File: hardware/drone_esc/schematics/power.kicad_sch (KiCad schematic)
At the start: 0 parts

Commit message: created power schematics, assigned footprints and parts
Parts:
- added C1, C2: 22uF 25V X7R MLCC, Capacitor_SMD:C_1210_3225Metric, symbol Device:C
- added C3: 100nF 10V X7R MLCC, Capacitor_SMD:C_0402_1005Metric, symbol Device:C
- added C4: 1nF 10V X7R MLCC, Capacitor_SMD:C_0402_1005Metric, symbol Device:C
- added R1: 1k, Resistor_SMD:R_0402_1005Metric, symbol Device:R
- added U1: AMS1117-3.3, Package_TO_SOT_SMD:SOT-223-3_TabPin2, symbol Regulator_Linear:AMS1117-3.3
- added U2: INA180A3, Package_TO_SOT_SMD:SOT-23-5, symbol Amplifier_Current:INA180A3
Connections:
- new net: C4.1, R1.2
- new net: R1.1, U2.1
- new net +3.3V: C2.1, C3.1, U1.2 (VO), U2.5 (V+)
- new net GND: C1.2, C2.2, C3.2, C4.2, U1.1 (GND), U2.2 (GND), U2.4 (-)
- new net VCC: C1.1, U1.3 (VI), U2.3 (+)
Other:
- note added: "100A: P = I^{2}R = 100A^{2} 0.00025 = 100A: 0.00025 100 ="
- note added: "Current Sense"
- note added: "Linear regulator (VCC to 3.3v)"
- note added: "Power"
- note added: "VCC = 4S"

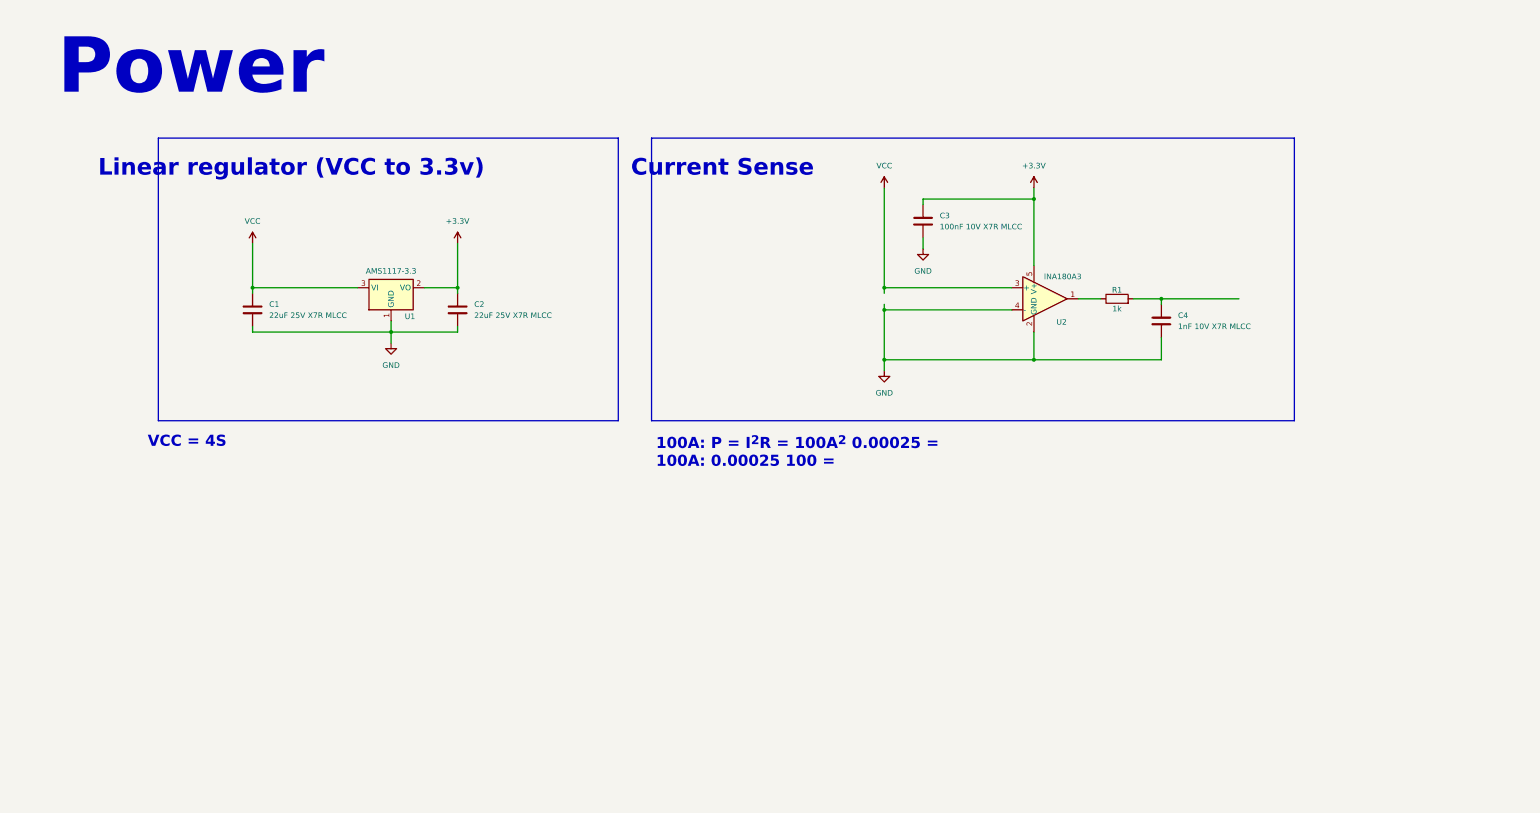
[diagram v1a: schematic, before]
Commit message: finished power section and one esc. need to finish the component assinment for jlcpcb and the rest of the esc
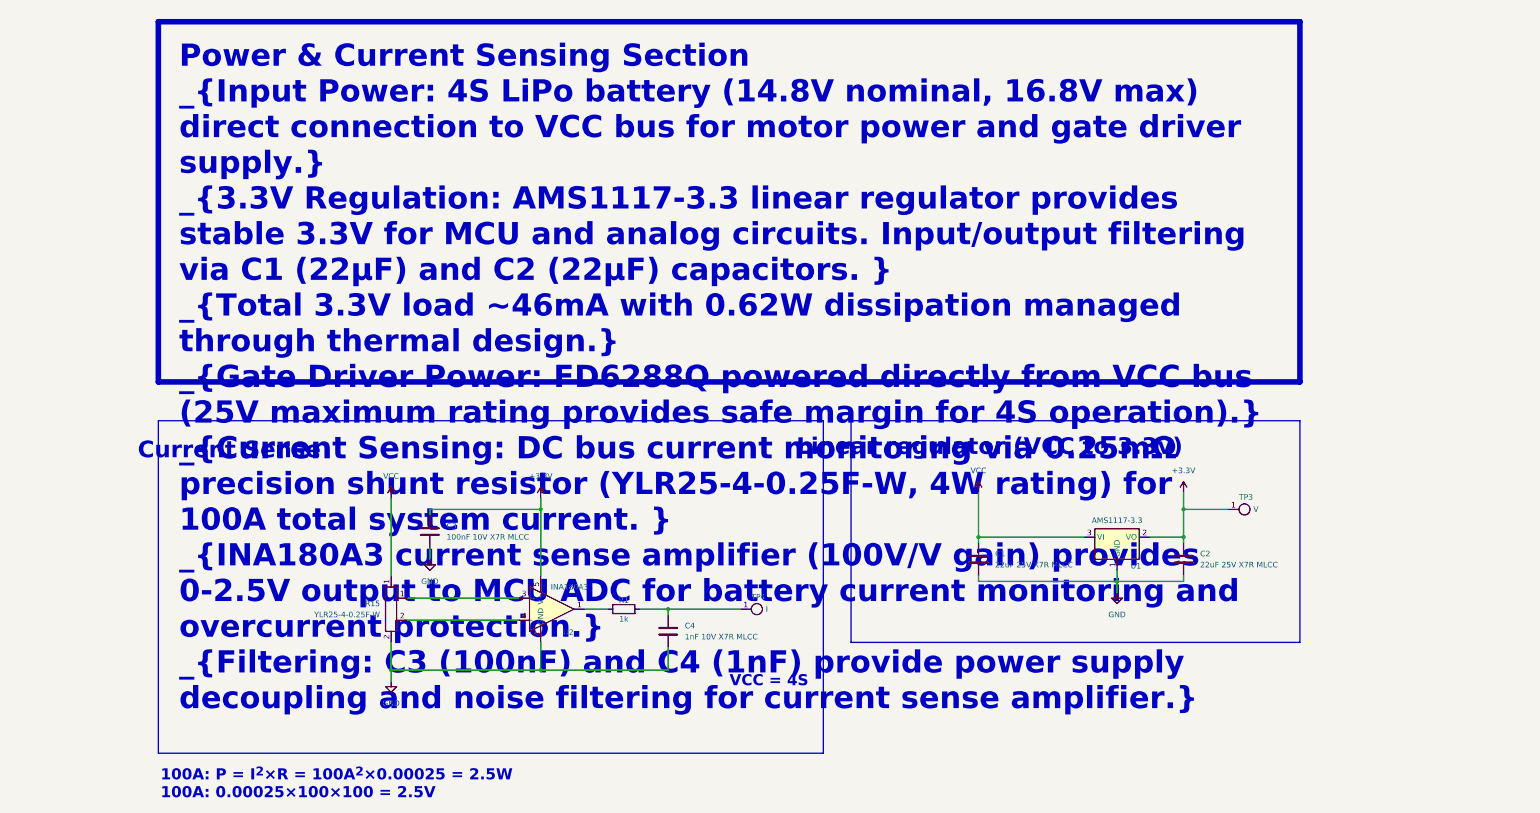
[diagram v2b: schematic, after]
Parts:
- added R15: YLR25-4-0.25F-W, Drone_components:YLR25-4-0.25F-W, symbol Drone_components:YLR25-4-0.25F-W
- added TP3: V, Drone_components:Rectangle test point, symbol Drone_components:Rectangle_test_point
- added TP4: I, Drone_components:Rectangle test point, symbol Drone_components:Rectangle_test_point
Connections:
- net +3.3V: now also TP3.1
- net GND: now also R15.2; no longer U2.4 (-)
- net VCC: now also R15.1; no longer U2.3 (+)
- net at C4.1, R1.2: now also TP4.1
- new net: R15.1, U2.3 (+)
- new net: R15.2, U2.4 (-)
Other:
- note added: "100A: P = I^{2}×R = 100A^{2}×0.00025 = 2.5W 100A: 0.00025×100×100 = 2.5V"
- note removed: "100A: P = I^{2}R = 100A^{2} 0.00025 = 100A: 0.00025 100 ="
- note removed: "Power"
- moved on the sheet: C1, C2, C3, C4, R1, U1, U2

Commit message: continued developing the pcb board
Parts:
- C1, C2: value 22uF 25V X7R MLCC -> 22uF 25V X5R MLCC; JLCPCB part C309062 -> C12891
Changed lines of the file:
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@@
+	)
+	(symbol
+		(lib_id "Device:C")
+		(at 252.73 140.97 0)
+		(unit 1)
+		(exclude_from_sim no)
+		(in_bom yes)
+		(on_board yes)
+		(dnp no)
+		(fields_autoplaced yes)
+		(property "Reference" "C2"
+			(at 256.54 139.6999 0)
+			(effects
+				(font
+					(size 1.27 1.27)
+				)
+				(justify left)
+			)
+		)
+		(property "Value" "22uF 25V X5R MLCC"
+			(at 256.54 142.2399 0)
+			(effects
+				(font
+					(size 1.27 1.27)
+				)
+				(justify left)
+			)
+		)
+		(property "Footprint" "Capacitor_SMD:C_1210_3225Metric"
+			(at 253.6952 144.78 0)
+			(effects
+				(font
+					(size 1.27 1.27)
+				)
+				(hide yes)
+			)
+		)
+		(property "Datasheet" "~"
+			(at 252.73 140.97 0)
+			(effects
+				(font
+					(size 1.27 1.27)
+				)
+				(hide yes)
+			)
+		)
+		(property "Description" "Unpolarized capacitor"
+			(at 252.73 140.97 0)
+			(effects
+				(font
+					(size 1.27 1.27)
+				)
+				(hide yes)
+			)
+		)
+		(property "JLCPCB part" "C12891"
+			(at 252.73 140.97 0)
+			(effects
+				(font
+					(size 1.27 1.27)
+				)
+				(hide yes)
+			)
+		)
+		(pin "2"
+		)
+		(pin "1"
+		)
+		(instances
+			(project "drone_esc"
+				(path "/b5a13fd4-6868-4fff-a56c-eae40f1d53c7/2b3d35f8-ad3a-479e-afa3-88f04276a871"
+					(reference "C2")
+					(unit 1)
+				)
+			)
+		)
 	)
 	(symbol
@@
 	(symbol
 		(lib_id "Device:C")
+		(at 205.74 140.97 0)
+		(unit 1)
+		(exclude_from_sim no)
+		(in_bom yes)
+		(on_board yes)
+		(dnp no)
+		(fields_autoplaced yes)
+		(property "Reference" "C1"
+			(at 209.55 139.6999 0)
+			(effects
+				(font
+					(size 1.27 1.27)
+				)
+				(justify left)
+			)
+		)
+		(property "Value" "22uF 25V X5R MLCC"
+			(at 209.55 142.2399 0)
+			(effects
+				(font
+					(size 1.27 1.27)
+				)
+				(justify left)
+			)
+		)
+		(property "Footprint" "Capacitor_SMD:C_1210_3225Metric"
+			(at 206.7052 144.78 0)
+			(effects
+				(font
+					(size 1.27 1.27)
+				)
+				(hide yes)
+			)
+		)
+		(property "Datasheet" "~"
+			(at 205.74 140.97 0)
+			(effects
+				(font
+					(size 1.27 1.27)
+				)
+				(hide yes)
+			)
+		)
+		(property "Description" "Unpolarized capacitor"
+			(at 205.74 140.97 0)
+			(effects
+				(font
+					(size 1.27 1.27)
+				)
+				(hide yes)
+			)
+		)
+		(property "JLCPCB part" "C12891"
+			(at 205.74 140.97 0)
+			(effects
+				(font
+					(size 1.27 1.27)
+				)
+				(hide yes)
+			)
+		)
+		(pin "2"
+		)
+		(pin "1"
+		)
+		(instances
+			(project "drone_esc"
+				(path "/b5a13fd4-6868-4fff-a56c-eae40f1d53c7/2b3d35f8-ad3a-479e-afa3-88f04276a871"
+					(reference "C1")
+					(unit 1)
+				)
+			)
+		)
+	)
+	(symbol
+		(lib_id "Device:C")
 		(at 134.62 157.48 0)
 		(unit 1)
@@
 	)
 	(symbol
-		(lib_id "Device:C")
-		(at 205.74 140.97 0)
-		(unit 1)
-		(exclude_from_sim no)
-		(in_bom yes)
-		(on_board yes)
-		(dnp no)
-		(fields_autoplaced yes)
-		(property "Reference" "C1"
-			(at 209.55 139.6999 0)
-			(effects
-				(font
-					(size 1.27 1.27)
-				)
-				(justify left)
-			)
-		)
-		(property "Value" "22uF 25V X7R MLCC"
-			(at 209.55 142.2399 0)
-			(effects
-				(font
-					(size 1.27 1.27)
-				)
-				(justify left)
-			)
-		)
-		(property "Footprint" "Capacitor_SMD:C_1210_3225Metric"
-			(at 206.7052 144.78 0)
-			(effects
-				(font
-					(size 1.27 1.27)
-				)
-				(hide yes)
-			)
-		)
-		(property "Datasheet" "https://lcsc.com/datasheet/lcsc_datasheet_2304140030_Samsung-Electro-Mechanics-CL32B226KAJNNNE_C309062.pdf"
-			(at 205.74 140.97 0)
-			(effects
-				(font
-					(size 1.27 1.27)
-				)
-				(hide yes)
-			)
-		)
-		(property "Description" "Unpolarized capacitor"
-			(at 205.74 140.97 0)
-			(effects
-				(font
-					(size 1.27 1.27)
-				)
-				(hide yes)
-			)
-		)
-		(property "JLCPCB part" "C309062"
-			(at 205.74 140.97 0)
-			(effects
-				(font
-					(size 1.27 1.27)
-				)
-				(hide yes)
-			)
-		)
-		(pin "1"
-		)
-		(pin "2"
-		)
-		(instances
-			(project ""
-				(path "/b5a13fd4-6868-4fff-a56c-eae40f1d53c7/2b3d35f8-ad3a-479e-afa3-88f04276a871"
-					(reference "C1")
-					(unit 1)
-				)
-			)
-		)
-	)
-	(symbol
 		(lib_id "Regulator_Linear:AMS1117-3.3")
 		(at 237.49 135.89 0)
@@
 					(unit 1)
 				)
-			)
-		)
-	)
-	(symbol
-		(lib_id "Device:C")
-		(at 252.73 140.97 0)
-		(unit 1)
-		(exclude_from_sim no)
-		(in_bom yes)
-		(on_board yes)
-		(dnp no)
-		(fields_autoplaced yes)
-		(property "Reference" "C2"
-			(at 256.54 139.6999 0)
-			(effects
-				(font
-					(size 1.27 1.27)
-				)
-				(justify left)
-			)
-		)
-		(property "Value" "22uF 25V X7R MLCC"
-			(at 256.54 142.2399 0)
-			(effects
-				(font
-					(size 1.27 1.27)
-				)
-				(justify left)
-			)
-		)
-		(property "Footprint" "Capacitor_SMD:C_1210_3225Metric"
-			(at 253.6952 144.78 0)
-			(effects
-				(font
-					(size 1.27 1.27)
-				)
-				(hide yes)
-			)
-		)
-		(property "Datasheet" "~"
-			(at 252.73 140.97 0)
-			(effects
-				(font
-					(size 1.27 1.27)
-				)
-				(hide yes)
-			)
-		)
-		(property "Description" "Unpolarized capacitor"
-			(at 252.73 140.97 0)
-			(effects
-				(font
-					(size 1.27 1.27)
-				)
-				(hide yes)
-			)
-		)
-		(property "JLCPCB part" "C309062"
-			(at 252.73 140.97 0)
-			(effects
-				(font
-					(size 1.27 1.27)
-				)
-				(hide yes)
-			)
-		)
-		(pin "1"
-		)
-		(pin "2"
-		)
-		(instances
-			(project "drone_esc"
-				(path "/b5a13fd4-6868-4fff-a56c-eae40f1d53c7/2b3d35f8-ad3a-479e-afa3-88f04276a871"
-					(reference "C2")
-					(unit 1)
-				)

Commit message: finnished component placement
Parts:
- added TP11: V, Drone_components:Rectangle test point, symbol Drone_components:Rectangle_test_point
- C3, C4, R1: Type (none) -> Basic
- R15: value YLR25-4-0.25F-W -> ~
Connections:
- net GND: now also U2.4 (-), TP11.1
- net VCC: now also U2.3 (+)

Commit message: replaced some of the schematics
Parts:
- C1, C2: footprint Capacitor_SMD:C_1210_3225Metric -> Capacitor_SMD:C_0805_2012Metric; JLCPCB part C12891 -> C45783
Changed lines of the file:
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@@
 			)
 		)
-		(property "Footprint" "Capacitor_SMD:C_1210_3225Metric"
+		(property "Footprint" "Capacitor_SMD:C_0805_2012Metric"
 			(at 253.6952 144.78 0)
 			(effects
@@
 			)
 		)
-		(property "JLCPCB part" "C12891"
+		(property "JLCPCB part" "C45783"
 			(at 252.73 140.97 0)
 			(effects
@@
 			)
 		)
-		(property "Footprint" "Capacitor_SMD:C_1210_3225Metric"
+		(property "Footprint" "Capacitor_SMD:C_0805_2012Metric"
 			(at 206.7052 144.78 0)
 			(effects
@@
 			)
 		)
-		(property "JLCPCB part" "C12891"
+		(property "JLCPCB part" "C45783"
 			(at 205.74 140.97 0)
 			(effects
